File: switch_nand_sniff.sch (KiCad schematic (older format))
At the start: 7 parts, among them P1 CONN_02X15, P2 CONN_02X15, P3 CONN_01X02, P4 CONN_01X02

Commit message: Add sip-8. staging before rollback to find resistor desired.
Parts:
- removed P3, P4: CONN_01X02, Pin_Headers:Pin_Header_Straight_1x02_Pitch2.00mm, symbol CONN_01X02
- removed R1, R2, R3: 0 Ohms, Resistors_SMD:R_0603_HandSoldering, symbol R_Small
- added P3, P4: CONN_01X08, switch:SIP-8, symbol CONN_01X08
- added R?: R_Small, symbol R_Small
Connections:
- net +3V3: now also P4.5 (P5)
- net GND: now also P3.1 (P1), P4.1 (P1)
- net at P1.1 (P1), P1.30 (P30), P2.1 (P1)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: now also P3.5 (P5)
- net at P1.11 (P11), P2.11 (P11): now also P4.3 (P3)
- net at P1.13 (P13), P2.13 (P13): now also P4.4 (P4)
- net at P1.19 (P19), P2.19 (P19): now also P4.6 (P6)
- net at P1.21 (P21), P2.21 (P21): now also P4.7 (P7)
- net at P1.23 (P23), P2.23 (P23): now also P4.8 (P8)
- net at P1.25 (P25), P2.25 (P25): now also P3.8 (P8)
- net at P1.27 (P27), P2.27 (P27): now also P3.7 (P7)
- net at P1.29 (P29), P2.29 (P29): now also P3.6 (P6)
- net at P1.3 (P3), P2.3 (P3): now also P3.4 (P4)
- net at P1.5 (P5), P2.5 (P5): now also P3.3 (P3)
- net at P1.7 (P7), P2.7 (P7): now also P3.2 (P2)
- net at P1.9 (P9), P2.9 (P9): now also P4.2 (P2)
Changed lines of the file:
@@
 	3300 3400 4700 3400
 Wire Wire Line
-	4700 3500 3300 3500
+	3300 3500 4700 3500
 Wire Wire Line
 	3300 3600 4700 3600
@@
 	4700 4200 3300 4200
 Wire Wire Line
-	3300 4300 4700 4300
-Wire Wire Line
 	3300 4400 4700 4400
 Wire Wire Line
@@
 	3300 4600 4700 4600
 Wire Wire Line
-	4700 3200 4700 2900
-Wire Wire Line
-	4700 2900 5750 2900
-Wire Wire Line
 	5750 2150 5750 4600
 Wire Wire Line
@@
 	5200 3200 5400 3200
 Wire Wire Line
-	5400 3200 5400 4750
+	5400 3200 5400 5250
 Wire Wire Line
 	5400 4500 5200 4500
@@
 	3300 3900 4700 3900
 Wire Wire Line
-	2800 3900 2700 3900
-Wire Wire Line
-	2700 3900 2700 2750
+	2700 3900 2800 3900
+Wire Wire Line
+	2700 1600 2700 3900
 Wire Wire Line
 	2700 2750 5300 2750
@@
 Connection ~ 2500 4500
 Wire Wire Line
-	3300 4000 3550 4000
-Wire Wire Line
-	3550 4000 3550 4750
-Connection ~ 3550 4750
-Wire Wire Line
-	4700 4000 4450 4000
-Wire Wire Line
-	4450 4000 4450 4750
-Connection ~ 4450 4750
-$Comp
-L GND #PWR01
-U 1 1 599BAC3C
-P 3750 5900
-F 0 "#PWR01" H 3750 5650 50  0001 C CNN
-F 1 "GND" H 3750 5750 50  0000 C CNN
-F 2 "" H 3750 5900 50  0000 C CNN
-F 3 "" H 3750 5900 50  0000 C CNN
-	1    3750 5900
-	1    0    0    -1
-$EndComp
-Wire Wire Line
-	3750 4750 3750 5900
-Connection ~ 3750 4750
+	3300 4000 3350 4000
+Wire Wire Line
+	3350 4000 3350 4750
+Connection ~ 3350 4750
+Wire Wire Line
+	4700 4000 4650 4000
+Wire Wire Line
+	4650 4000 4650 4750
+Connection ~ 4650 4750
+Connection ~ 5400 4750
 Connection ~ 5400 4000
 Connection ~ 5400 3800
 $Comp
-L +3.3V #PWR02
+L +3.3V #PWR01
 U 1 1 599BADE4
-P 3600 2500
-F 0 "#PWR02" H 3600 2350 50  0001 C CNN
-F 1 "+3.3V" H 3600 2640 50  0000 C CNN
-F 2 "" H 3600 2500 50  0000 C CNN
-F 3 "" H 3600 2500 50  0000 C CNN
-	1    3600 2500
-	1    0    0    -1
-$EndComp
-Wire Wire Line
-	3600 2500 3600 2750
-Connection ~ 3600 2750
-Wire Wire Line
-	5750 2150 2350 2150
+P 2700 1600
+F 0 "#PWR01" H 2700 1450 50  0001 C CNN
+F 1 "+3.3V" H 2700 1740 50  0000 C CNN
+F 2 "" H 2700 1600 50  0000 C CNN
+F 3 "" H 2700 1600 50  0000 C CNN
+	1    2700 1600
+	1    0    0    -1
+$EndComp
+Connection ~ 2700 2750
+Wire Wire Line
+	2350 2150 5750 2150
 Connection ~ 2350 2900
+$Comp
+L GND #PWR02
+U 1 1 59AB99FC
+P 5400 5250
+F 0 "#PWR02" H 5400 5000 50  0001 C CNN
+F 1 "GND" H 5400 5100 50  0000 C CNN
+F 2 "" H 5400 5250 50  0000 C CNN
+F 3 "" H 5400 5250 50  0000 C CNN
+	1    5400 5250
+	1    0    0    -1
+$EndComp
+$Comp
+L CONN_01X08 P3
+U 1 1 59AB9B20
+P 3850 1200
+F 0 "P3" H 3850 1650 50  0000 C CNN
+F 1 "CONN_01X08" V 3950 1200 50  0000 C CNN
+F 2 "switch:SIP-8" H 3850 1200 50  0000 C CNN
+F 3 "" H 3850 1200 50  0000 C CNN
+	1    3850 1200
+	0    -1   -1   0
+$EndComp
+$Comp
+L CONN_01X08 P4
+U 1 1 59AB9BC3
+P 3700 5900
+F 0 "P4" H 3700 6350 50  0000 C CNN
+F 1 "CONN_01X08" V 3800 5900 50  0000 C CNN
+F 2 "switch:SIP-8" H 3700 5900 50  0000 C CNN
+F 3 "" H 3700 5900 50  0000 C CNN
+	1    3700 5900
+	0    -1   1    0
+$EndComp
+Wire Wire Line
+	3300 4300 4700 4300
+Wire Wire Line
+	4550 4400 4550 1800
+Wire Wire Line
+	4550 1800 4200 1800
+Wire Wire Line
+	4200 1800 4200 1400
+Connection ~ 4550 4400
+Wire Wire Line
+	4500 4500 4500 1900
+Wire Wire Line
+	4500 1900 4100 1900
+Wire Wire Line
+	4100 1900 4100 1400
+Connection ~ 4500 4500
+Wire Wire Line
+	4450 4600 4450 2000
+Wire Wire Line
+	4450 2000 4000 2000
+Wire Wire Line
+	4000 2000 4000 1400
+Connection ~ 4450 4600
+Wire Wire Line
+	3900 1400 3900 2150
+Connection ~ 3900 2150
+Wire Wire Line
+	4400 3300 4400 2250
+Connection ~ 4400 3300
+Wire Wire Line
+	4400 2250 3800 2250
 Connection ~ 5750 2900
-$Comp
-L CONN_01X02 P3
-U 1 1 599D1913
-P 4800 1100
-F 0 "P3" H 4800 1250 50  0000 C CNN
-F 1 "CONN_01X02" V 4900 1100 50  0000 C CNN
-F 2 "Pin_Headers:Pin_Header_Straight_1x02_Pitch2.00mm" H 4800 1100 50  0000 C CNN
-F 3 "" H 4800 1100 50  0000 C CNN
-	1    4800 1100
-	1    0    0    -1
-$EndComp
-$Comp
-L CONN_01X02 P4
-U 1 1 599D19F1
-P 5050 5550
-F 0 "P4" H 5050 5700 50  0000 C CNN
-F 1 "CONN_01X02" V 5150 5550 50  0000 C CNN
-F 2 "Pin_Headers:Pin_Header_Straight_1x02_Pitch2.00mm" H 5050 5550 50  0000 C CNN
-F 3 "" H 5050 5550 50  0000 C CNN
-	1    5050 5550
-	1    0    0    -1
-$EndComp
-Wire Wire Line
-	4600 5500 4850 5500
-Connection ~ 4600 3300
-Wire Wire Line
-	3750 5600 4850 5600
-Connection ~ 3750 5600
-Connection ~ 3450 4500
-Connection ~ 4200 4300
-$Comp
-L R_Small R1
-U 1 1 599D1FA2
-P 4600 5300
-F 0 "R1" H 4630 5320 50  0000 L CNN
-F 1 "0 Ohms" H 4630 5260 50  0000 L CNN
-F 2 "Resistors_SMD:R_0603_HandSoldering" H 4600 5300 50  0000 C CNN
-F 3 "" H 4600 5300 50  0000 C CNN
-	1    4600 5300
-	1    0    0    -1
-$EndComp
-Wire Wire Line
-	4600 5400 4600 5500
-Wire Wire Line
-	4600 3300 4600 5200
-Wire Wire Line
-	4600 5100 4750 5100
-Wire Wire Line
-	4750 5100 4750 5500
-Connection ~ 4750 5500
-Connection ~ 4600 5100
-Wire Wire Line
-	4200 4300 4200 1150
-Wire Wire Line
-	4200 1150 4600 1150
-Wire Wire Line
-	3450 4500 3450 1050
-Wire Wire Line
-	3450 1050 4600 1050
-$Comp
-L R_Small R3
-U 1 1 599DE5B4
-P 4050 1650
-F 0 "R3" H 4080 1670 50  0000 L CNN
-F 1 "0 Ohms" H 4080 1610 50  0000 L CNN
-F 2 "Resistors_SMD:R_0603_HandSoldering" H 4050 1650 50  0000 C CNN
-F 3 "" H 4050 1650 50  0000 C CNN
-	1    4050 1650
-	1    0    0    -1
-$EndComp
-$Comp
-L R_Small R2
-U 1 1 599DE684
-P 3250 1650
-F 0 "R2" H 3280 1670 50  0000 L CNN
-F 1 "0 Ohms" H 3280 1610 50  0000 L CNN
-F 2 "Resistors_SMD:R_0603_HandSoldering" H 3250 1650 50  0000 C CNN
-F 3 "" H 3250 1650 50  0000 C CNN
-	1    3250 1650
-	1    0    0    -1
-$EndComp
-Wire Wire Line
-	4050 1550 4050 1450
-Wire Wire Line
-	4050 1450 4200 1450
-Connection ~ 4200 1450
-Wire Wire Line
-	4050 1750 4050 1900
-Wire Wire Line
-	4050 1900 4200 1900
-Connection ~ 4200 1900
-Wire Wire Line
-	3250 1550 3250 1400
-Wire Wire Line
-	3250 1400 3450 1400
-Connection ~ 3450 1400
-Wire Wire Line
-	3250 1750 3250 1900
-Wire Wire Line
-	3250 1900 3450 1900
-Connection ~ 3450 1900
+Wire Wire Line
+	4700 2900 4700 3200
+Wire Wire Line
+	4700 2900 5750 2900
+Wire Wire Line
+	3800 2250 3800 1400
+Wire Wire Line
+	3700 1400 3700 2350
+Wire Wire Line
+	3700 2350 4350 2350
+Wire Wire Line
+	4350 2350 4350 3400
+Connection ~ 4350 3400
+Wire Wire Line
+	3600 1400 3600 2450
+Wire Wire Line
+	3600 2450 4300 2450
+Wire Wire Line
+	4300 2450 4300 3500
+Connection ~ 4300 3500
+$Comp
+L GND #PWR03
+U 1 1 59ABAC3D
+P 3300 1800
+F 0 "#PWR03" H 3300 1550 50  0001 C CNN
+F 1 "GND" H 3300 1650 50  0000 C CNN
+F 2 "" H 3300 1800 50  0000 C CNN
+F 3 "" H 3300 1800 50  0000 C CNN
+	1    3300 1800
+	1    0    0    -1
+$EndComp
+Wire Wire Line
+	3500 1400 3500 1600
+Wire Wire Line
+	3500 1600 3300 1600
+Wire Wire Line
+	3300 1600 3300 1800
+$Comp
+L GND #PWR04
+U 1 1 59ABAD1B
+P 2800 5950
+F 0 "#PWR04" H 2800 5700 50  0001 C CNN
+F 1 "GND" H 2800 5800 50  0000 C CNN
+F 2 "" H 2800 5950 50  0000 C CNN
+F 3 "" H 2800 5950 50  0000 C CNN
+	1    2800 5950
+	1    0    0    -1
+$EndComp
+Wire Wire Line
+	3350 5700 3350 5400
+Wire Wire Line
+	3350 5400 2800 5400
+Wire Wire Line
+	2800 5400 2800 5950
+Wire Wire Line
+	3450 5700 3450 3600
+Connection ~ 3450 3600
+Wire Wire Line
+	3550 5700 3550 3700
+Connection ~ 3550 3700
+Wire Wire Line
+	3650 5700 3650 3800
+Connection ~ 3650 3800
+Wire Wire Line
+	3750 5700 3750 3900
+Connection ~ 3750 3900
+Wire Wire Line
+	3850 5700 3850 4100
+Connection ~ 3850 4100
+Wire Wire Line
+	3950 5700 3950 4200
+Connection ~ 3950 4200
+Wire Wire Line
+	4050 5700 4050 4300
+Connection ~ 4050 4300
+$Comp
+L R_Small R?
+U 1 1 59ABBED3
+P 3250 550
+F 0 "R?" H 3280 570 50  0000 L CNN
+F 1 "R_Small" H 3280 510 50  0000 L CNN
+F 2 "" H 3250 550 50  0000 C CNN
+F 3 "" H 3250 550 50  0000 C CNN
+	1    3250 550
+	1    0    0    -1
+$EndComp
 $EndSCHEMATC

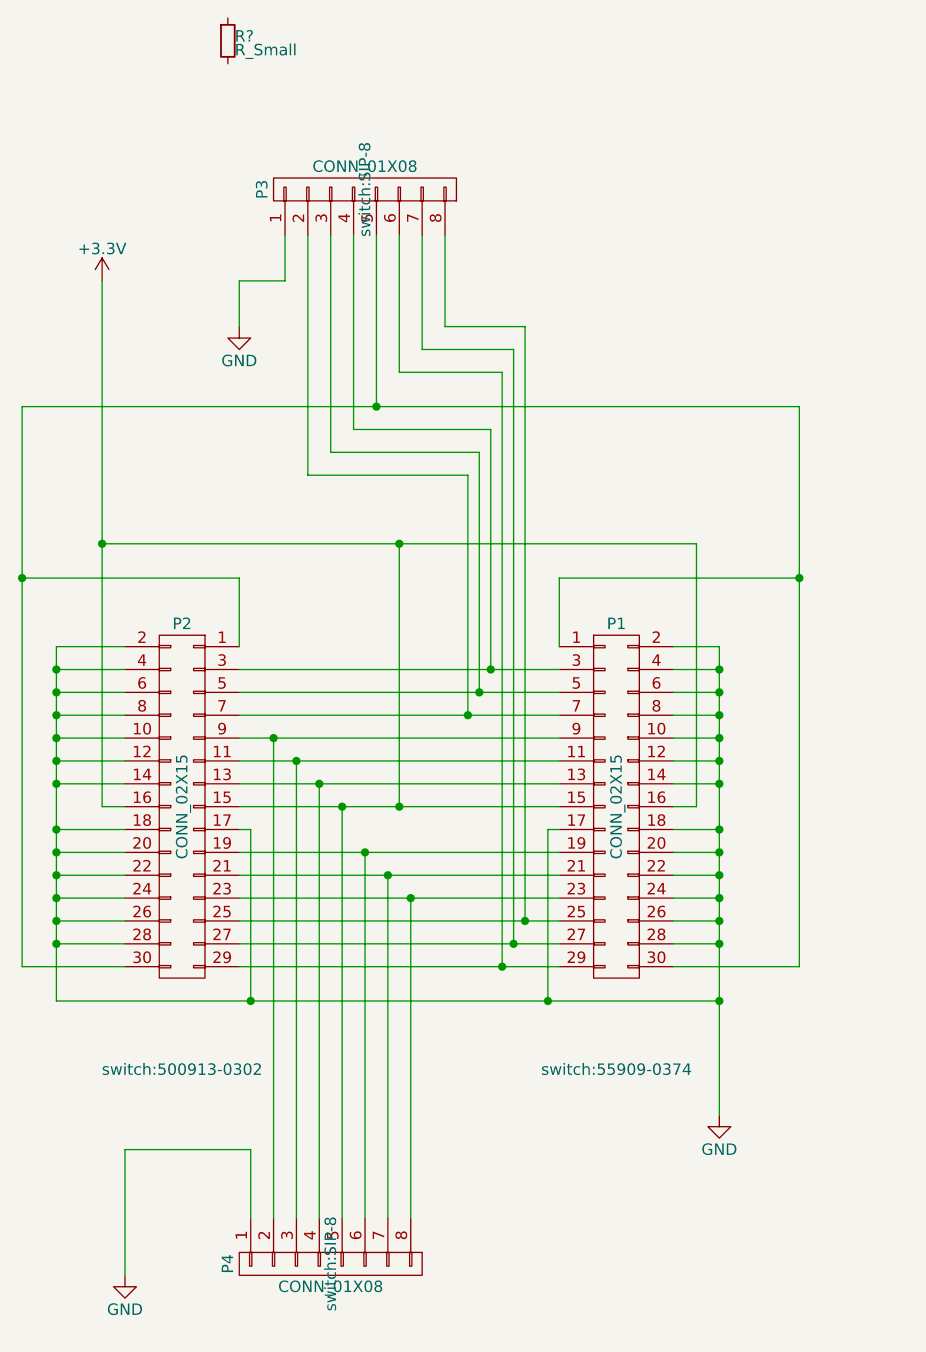
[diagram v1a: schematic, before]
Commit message: Added derefelection resistors, still needs matched-length routing.
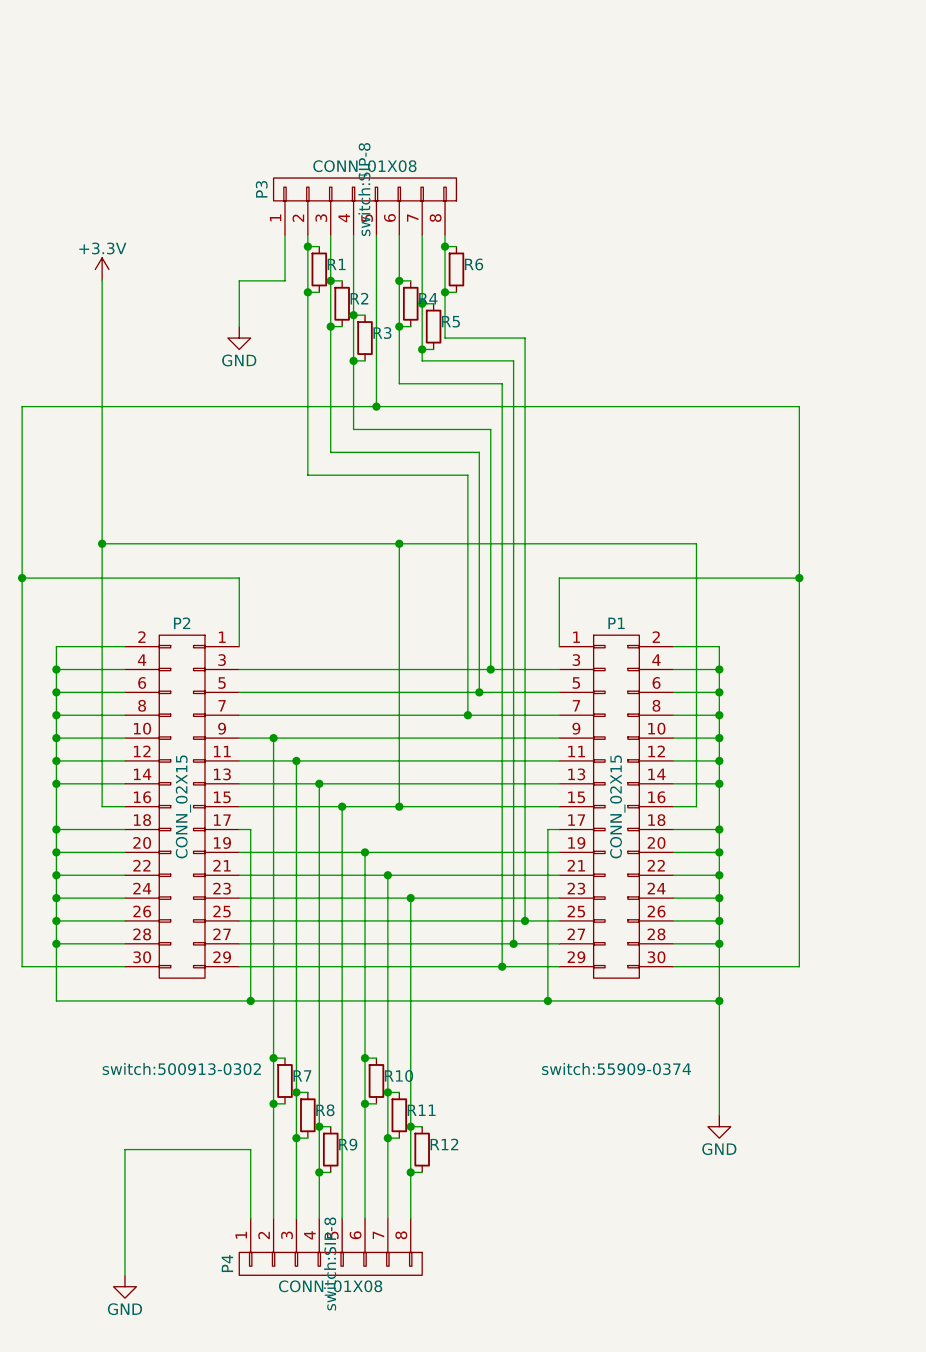
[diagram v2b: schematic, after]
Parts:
- removed R?: R_Small, symbol R_Small
- added R1, R10, R11, R12, R2, R3, R4, R5, R6, R7, R8, R9: 500 Ohms, Resistors_SMD:R_0603, symbol R_Small
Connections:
- net at P1.11 (P11), P2.11 (P11), P4.3 (P3): now also R8.1, R8.2
- net at P1.13 (P13), P2.13 (P13), P4.4 (P4): now also R9.1, R9.2
- net at P1.19 (P19), P2.19 (P19), P4.6 (P6): now also R10.1, R10.2
- net at P1.21 (P21), P2.21 (P21), P4.7 (P7): now also R11.1, R11.2
- net at P1.23 (P23), P2.23 (P23), P4.8 (P8): now also R12.1, R12.2
- net at P1.25 (P25), P2.25 (P25), P3.8 (P8): now also R6.1, R6.2
- net at P1.27 (P27), P2.27 (P27), P3.7 (P7): now also R5.1, R5.2
- net at P1.29 (P29), P2.29 (P29), P3.6 (P6): now also R4.1, R4.2
- net at P1.3 (P3), P2.3 (P3), P3.4 (P4): now also R3.1, R3.2
- net at P1.5 (P5), P2.5 (P5), P3.3 (P3): now also R2.1, R2.2
- net at P1.7 (P7), P2.7 (P7), P3.2 (P2): now also R1.1, R1.2
- net at P1.9 (P9), P2.9 (P9), P4.2 (P2): now also R7.1, R7.2
